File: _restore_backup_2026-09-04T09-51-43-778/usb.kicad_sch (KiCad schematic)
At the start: 29 parts, among them J3 USB4105-GF-A, U11 TPD4E05U06QDQARQ1, U5 FT230X, U8 NCP730BMT330

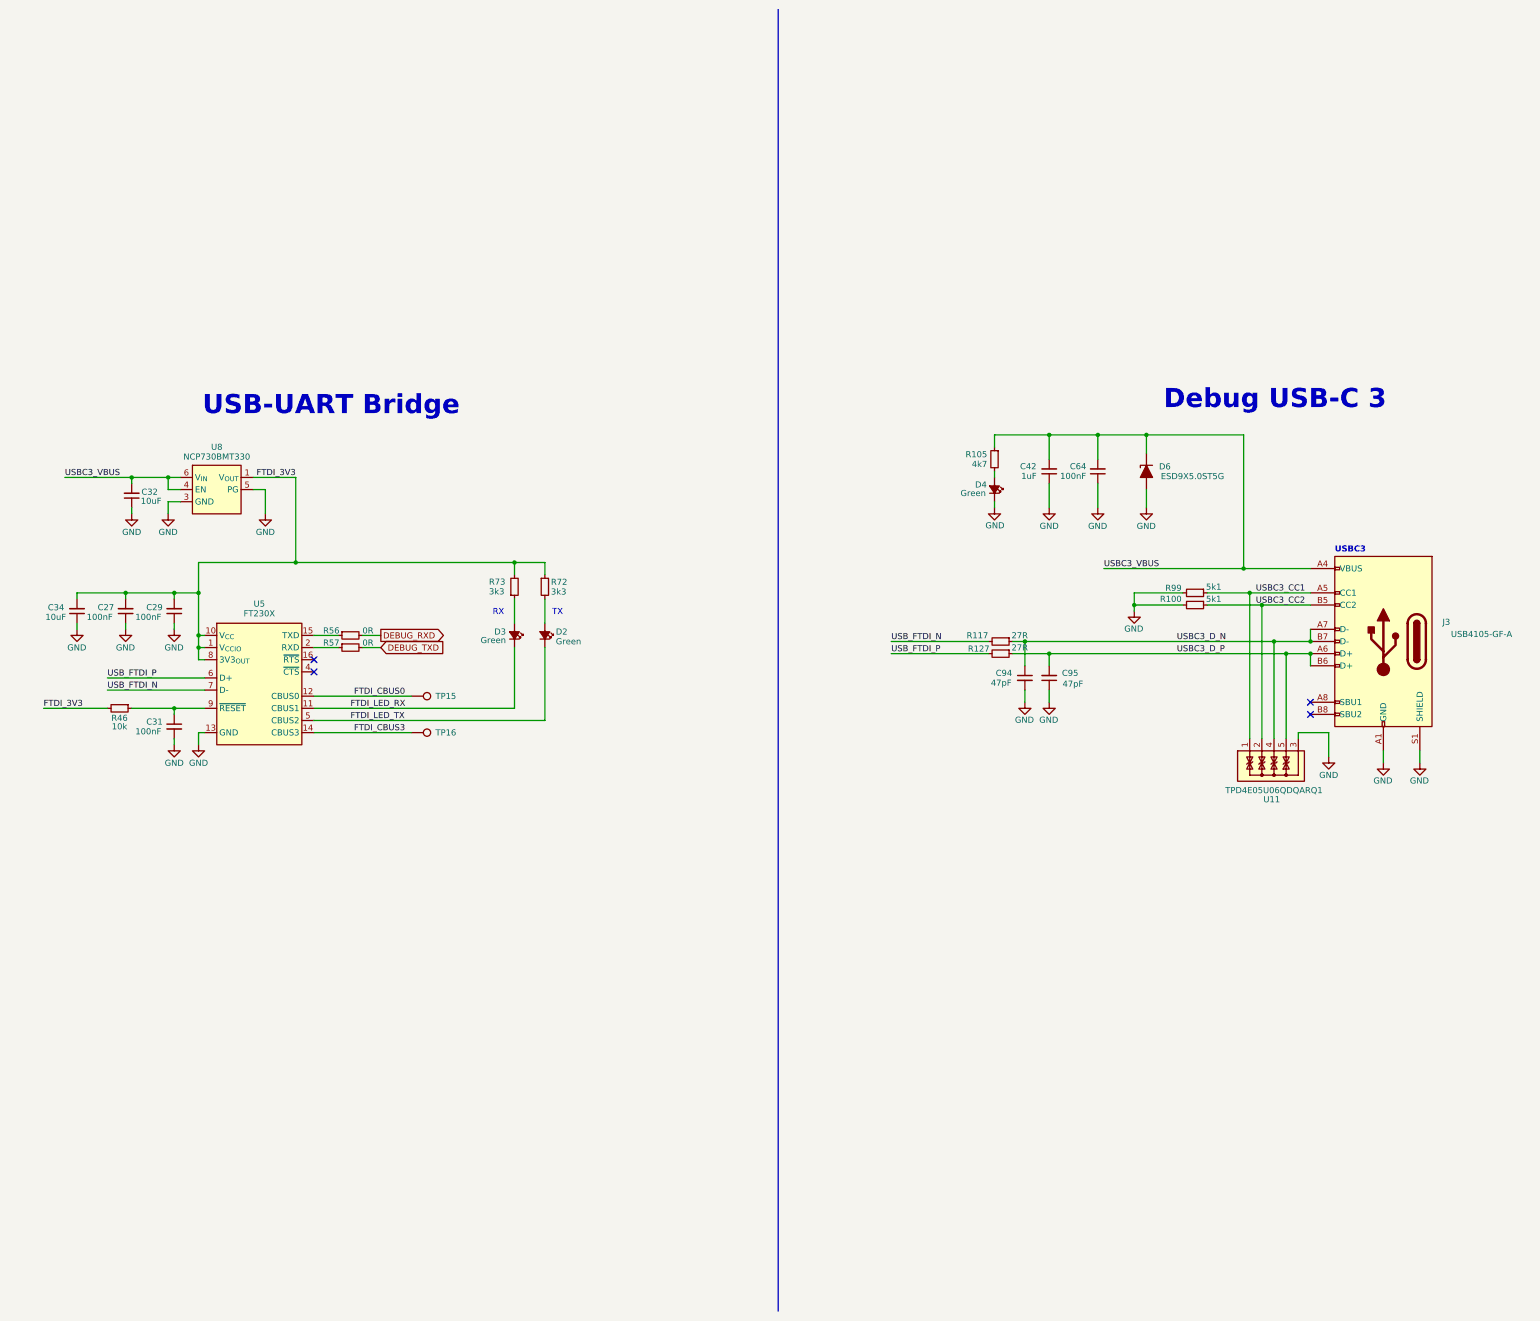
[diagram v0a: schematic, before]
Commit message: Add CSI, USB, HDMI, PCIe
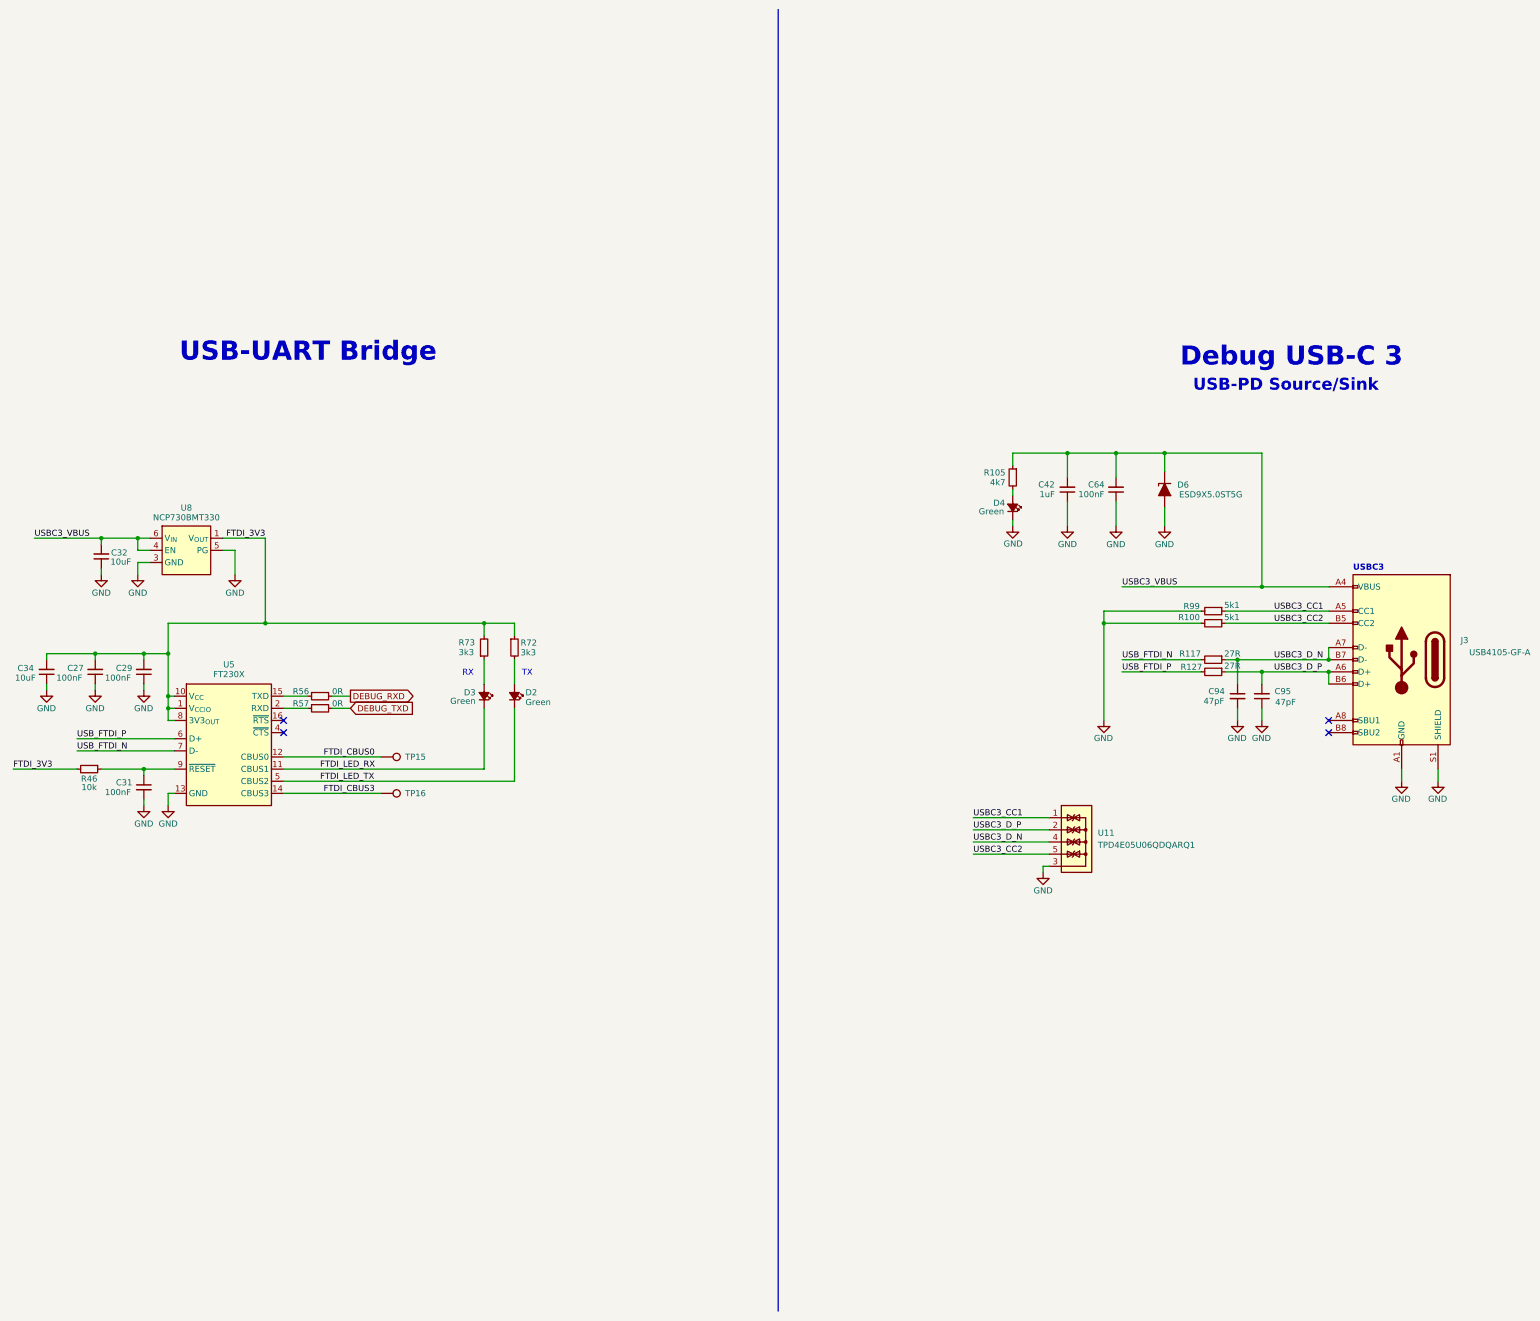
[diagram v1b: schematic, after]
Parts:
- U11: footprint Argus-Miscellaneous:USON-10_TEX -> JetsonCarrier:USON-10_2.5x1mm_P0.5mm
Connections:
- net USBC3_CC2: now also U11.5, U11.6; no longer U11.2, U11.9
- net USBC3_D_P: now also U11.2, U11.9; no longer U11.5, U11.6
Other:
- note added: "USB-PD Source/Sink"
